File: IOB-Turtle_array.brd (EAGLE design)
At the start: 104.1 x 106.7 mm, 49 parts

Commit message: Added missing values
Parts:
- D1X11, D1X12, D1X13, D1X14: value (none) -> 4.7v
- R1X11, R1X12, R1X13, R1X14, R2X11, R2X12, R2X13, R2X14, R3X11, R3X12, R3X13, R3X14: value (none) -> 10k
- R4X11, R4X12, R4X13, R4X14: value (none) -> 1k0
- R5X11, R5X12, R5X13, R5X14, R6X11, R6X12, R6X13, R6X14, R7X11, R7X12, R7X13, R7X14: value (none) -> 200R
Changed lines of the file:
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@@
 </autorouter>
 <elements>
-<element name="D1X11" library="SPCoast" package="SOT23-3" value="" x="63.5" y="12.7" rot="R180"/>
+<element name="D1X11" library="SPCoast" package="SOT23-3" value="4.7v" x="63.5" y="12.7" rot="R180"/>
 <element name="FID1X11" library="SPCoast" package="FIDUCIAL_1MM" value="" x="41.275" y="10.16"/>
 <element name="FID2X11" library="SPCoast" package="FIDUCIAL_1MM" value="" x="76.835" y="27.305"/>
 <element name="J1X11" library="SPCoast" package="RJ24-INVERTED-PINS" value="" x="32.385" y="17.78" rot="R90"/>
-<element name="R1X11" library="SPCoast" package="0805-RES" value="" x="58.42" y="24.13" rot="R270"/>
-<element name="R2X11" library="SPCoast" package="0805-RES" value="" x="54.61" y="24.13" rot="R270"/>
-<element name="R3X11" library="SPCoast" package="0805-RES" value="" x="50.8" y="24.13" rot="R270"/>
-<element name="R4X11" library="SPCoast" package="0805-RES" value="" x="54.61" y="12.7"/>
-<element name="R5X11" library="SPCoast" package="0805-RES" value="" x="43.18" y="19.05" rot="R180"/>
-<element name="R6X11" library="SPCoast" package="0805-RES" value="" x="43.18" y="16.51" rot="R180"/>
-<element name="R7X11" library="SPCoast" package="0805-RES" value="" x="43.18" y="21.59" rot="R180"/>
+<element name="R1X11" library="SPCoast" package="0805-RES" value="10k" x="58.42" y="24.13" rot="R270"/>
+<element name="R2X11" library="SPCoast" package="0805-RES" value="10k" x="54.61" y="24.13" rot="R270"/>
+<element name="R3X11" library="SPCoast" package="0805-RES" value="10k" x="50.8" y="24.13" rot="R270"/>
+<element name="R4X11" library="SPCoast" package="0805-RES" value="1k0" x="54.61" y="12.7"/>
+<element name="R5X11" library="SPCoast" package="0805-RES" value="200R" x="43.18" y="19.05" rot="R180"/>
+<element name="R6X11" library="SPCoast" package="0805-RES" value="200R" x="43.18" y="16.51" rot="R180"/>
+<element name="R7X11" library="SPCoast" package="0805-RES" value="200R" x="43.18" y="21.59" rot="R180"/>
 <element name="U$1X11" library="SPCoast" package="IO4-IOB" value="" x="25.4" y="8.89"/>
-<element name="D1X12" library="SPCoast" package="SOT23-3" value="" x="63.5" y="33.02" rot="R180"/>
+<element name="D1X12" library="SPCoast" package="SOT23-3" value="4.7v" x="63.5" y="33.02" rot="R180"/>
 <element name="FID1X12" library="SPCoast" package="FIDUCIAL_1MM" value="" x="41.275" y="30.48"/>
 <element name="FID2X12" library="SPCoast" package="FIDUCIAL_1MM" value="" x="76.835" y="47.625"/>
 <element name="J1X12" library="SPCoast" package="RJ24-INVERTED-PINS" value="" x="32.385" y="38.1" rot="R90"/>
-<element name="R1X12" library="SPCoast" package="0805-RES" value="" x="58.42" y="44.45" rot="R270"/>
-<element name="R2X12" library="SPCoast" package="0805-RES" value="" x="54.61" y="44.45" rot="R270"/>
-<element name="R3X12" library="SPCoast" package="0805-RES" value="" x="50.8" y="44.45" rot="R270"/>
-<element name="R4X12" library="SPCoast" package="0805-RES" value="" x="54.61" y="33.02"/>
-<element name="R5X12" library="SPCoast" package="0805-RES" value="" x="43.18" y="39.37" rot="R180"/>
-<element name="R6X12" library="SPCoast" package="0805-RES" value="" x="43.18" y="36.83" rot="R180"/>
-<element name="R7X12" library="SPCoast" package="0805-RES" value="" x="43.18" y="41.91" rot="R180"/>
+<element name="R1X12" library="SPCoast" package="0805-RES" value="10k" x="58.42" y="44.45" rot="R270"/>
+<element name="R2X12" library="SPCoast" package="0805-RES" value="10k" x="54.61" y="44.45" rot="R270"/>
+<element name="R3X12" library="SPCoast" package="0805-RES" value="10k" x="50.8" y="44.45" rot="R270"/>
+<element name="R4X12" library="SPCoast" package="0805-RES" value="1k0" x="54.61" y="33.02"/>
+<element name="R5X12" library="SPCoast" package="0805-RES" value="200R" x="43.18" y="39.37" rot="R180"/>
+<element name="R6X12" library="SPCoast" package="0805-RES" value="200R" x="43.18" y="36.83" rot="R180"/>
+<element name="R7X12" library="SPCoast" package="0805-RES" value="200R" x="43.18" y="41.91" rot="R180"/>
 <element name="U$1X12" library="SPCoast" package="IO4-IOB" value="" x="25.4" y="29.21"/>
-<element name="D1X13" library="SPCoast" package="SOT23-3" value="" x="63.5" y="53.34" rot="R180"/>
+<element name="D1X13" library="SPCoast" package="SOT23-3" value="4.7v" x="63.5" y="53.34" rot="R180"/>
 <element name="FID1X13" library="SPCoast" package="FIDUCIAL_1MM" value="" x="41.275" y="50.8"/>
 <element name="FID2X13" library="SPCoast" package="FIDUCIAL_1MM" value="" x="76.835" y="67.945"/>
 <element name="J1X13" library="SPCoast" package="RJ24-INVERTED-PINS" value="" x="32.385" y="58.42" rot="R90"/>
-<element name="R1X13" library="SPCoast" package="0805-RES" value="" x="58.42" y="64.77" rot="R270"/>
-<element name="R2X13" library="SPCoast" package="0805-RES" value="" x="54.61" y="64.77" rot="R270"/>
-<element name="R3X13" library="SPCoast" package="0805-RES" value="" x="50.8" y="64.77" rot="R270"/>
-<element name="R4X13" library="SPCoast" package="0805-RES" value="" x="54.61" y="53.34"/>
-<element name="R5X13" library="SPCoast" package="0805-RES" value="" x="43.18" y="59.69" rot="R180"/>
-<element name="R6X13" library="SPCoast" package="0805-RES" value="" x="43.18" y="57.15" rot="R180"/>
-<element name="R7X13" library="SPCoast" package="0805-RES" value="" x="43.18" y="62.23" rot="R180"/>
+<element name="R1X13" library="SPCoast" package="0805-RES" value="10k" x="58.42" y="64.77" rot="R270"/>
+<element name="R2X13" library="SPCoast" package="0805-RES" value="10k" x="54.61" y="64.77" rot="R270"/>
+<element name="R3X13" library="SPCoast" package="0805-RES" value="10k" x="50.8" y="64.77" rot="R270"/>
+<element name="R4X13" library="SPCoast" package="0805-RES" value="1k0" x="54.61" y="53.34"/>
+<element name="R5X13" library="SPCoast" package="0805-RES" value="200R" x="43.18" y="59.69" rot="R180"/>
+<element name="R6X13" library="SPCoast" package="0805-RES" value="200R" x="43.18" y="57.15" rot="R180"/>
+<element name="R7X13" library="SPCoast" package="0805-RES" value="200R" x="43.18" y="62.23" rot="R180"/>
 <element name="U$1X13" library="SPCoast" package="IO4-IOB" value="" x="25.4" y="49.53"/>
-<element name="D1X14" library="SPCoast" package="SOT23-3" value="" x="63.5" y="73.66" rot="R180"/>
+<element name="D1X14" library="SPCoast" package="SOT23-3" value="4.7v" x="63.5" y="73.66" rot="R180"/>
 <element name="FID1X14" library="SPCoast" package="FIDUCIAL_1MM" value="" x="41.275" y="71.12"/>
 <element name="FID2X14" library="SPCoast" package="FIDUCIAL_1MM" value="" x="76.835" y="88.265"/>
 <element name="J1X14" library="SPCoast" package="RJ24-INVERTED-PINS" value="" x="32.385" y="78.74" rot="R90"/>
-<element name="R1X14" library="SPCoast" package="0805-RES" value="" x="58.42" y="85.09" rot="R270"/>
-<element name="R2X14" library="SPCoast" package="0805-RES" value="" x="54.61" y="85.09" rot="R270"/>
-<element name="R3X14" library="SPCoast" package="0805-RES" value="" x="50.8" y="85.09" rot="R270"/>
-<element name="R4X14" library="SPCoast" package="0805-RES" value="" x="54.61" y="73.66"/>
-<element name="R5X14" library="SPCoast" package="0805-RES" value="" x="43.18" y="80.01" rot="R180"/>
-<element name="R6X14" library="SPCoast" package="0805-RES" value="" x="43.18" y="77.47" rot="R180"/>
-<element name="R7X14" library="SPCoast" package="0805-RES" value="" x="43.18" y="82.55" rot="R180"/>
+<element name="R1X14" library="SPCoast" package="0805-RES" value="10k" x="58.42" y="85.09" rot="R270"/>
+<element name="R2X14" library="SPCoast" package="0805-RES" value="10k" x="54.61" y="85.09" rot="R270"/>
+<element name="R3X14" library="SPCoast" package="0805-RES" value="10k" x="50.8" y="85.09" rot="R270"/>
+<element name="R4X14" library="SPCoast" package="0805-RES" value="1k0" x="54.61" y="73.66"/>
+<element name="R5X14" library="SPCoast" package="0805-RES" value="200R" x="43.18" y="80.01" rot="R180"/>
+<element name="R6X14" library="SPCoast" package="0805-RES" value="200R" x="43.18" y="77.47" rot="R180"/>
+<element name="R7X14" library="SPCoast" package="0805-RES" value="200R" x="43.18" y="82.55" rot="R180"/>
 <element name="U$1X14" library="SPCoast" package="IO4-IOB" value="" x="25.4" y="69.85"/>
 <element name="U$1X1" library="SPCoast" package="BOARD-DINRAIL-3.17IN-H4X-IOB" value="" x="0" y="0"/>

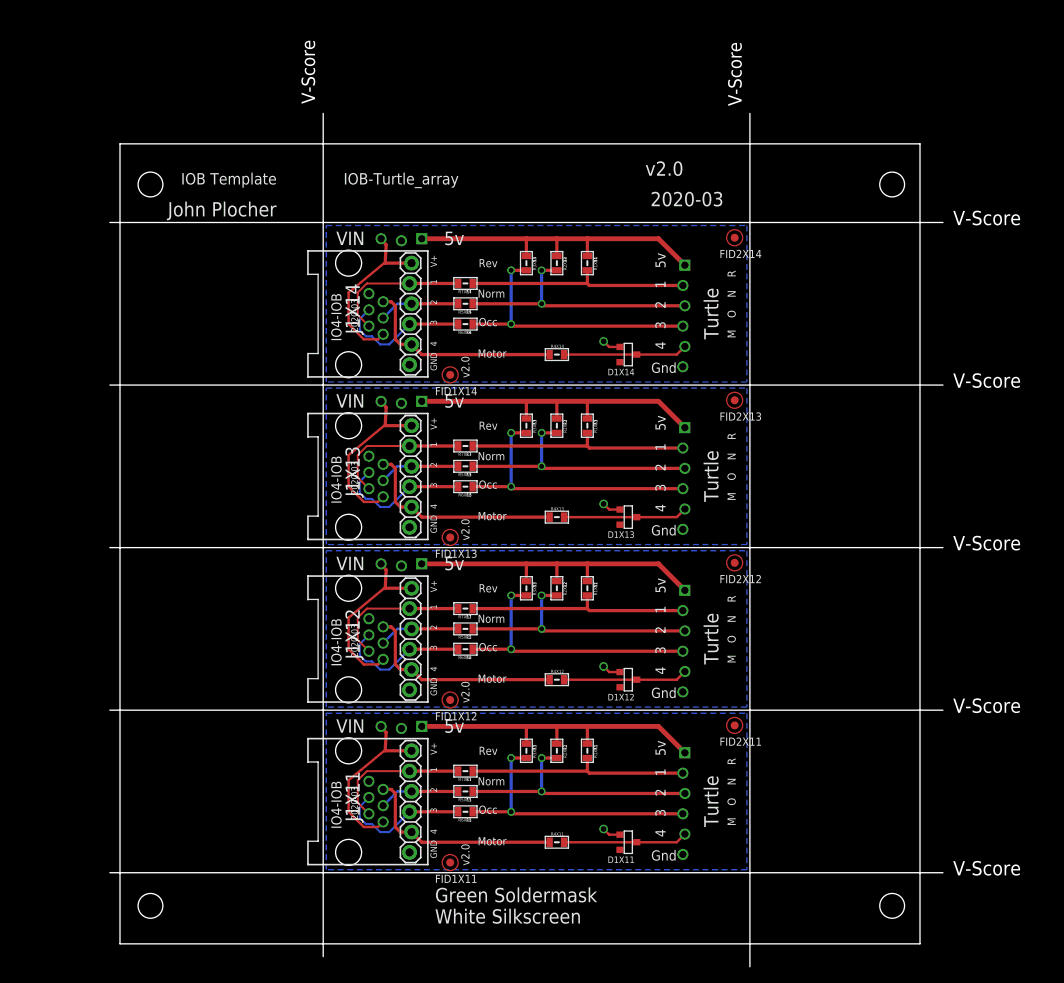
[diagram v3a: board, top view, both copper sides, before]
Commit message: add lpf on inputs, normalized silkscreen layout across IOBs
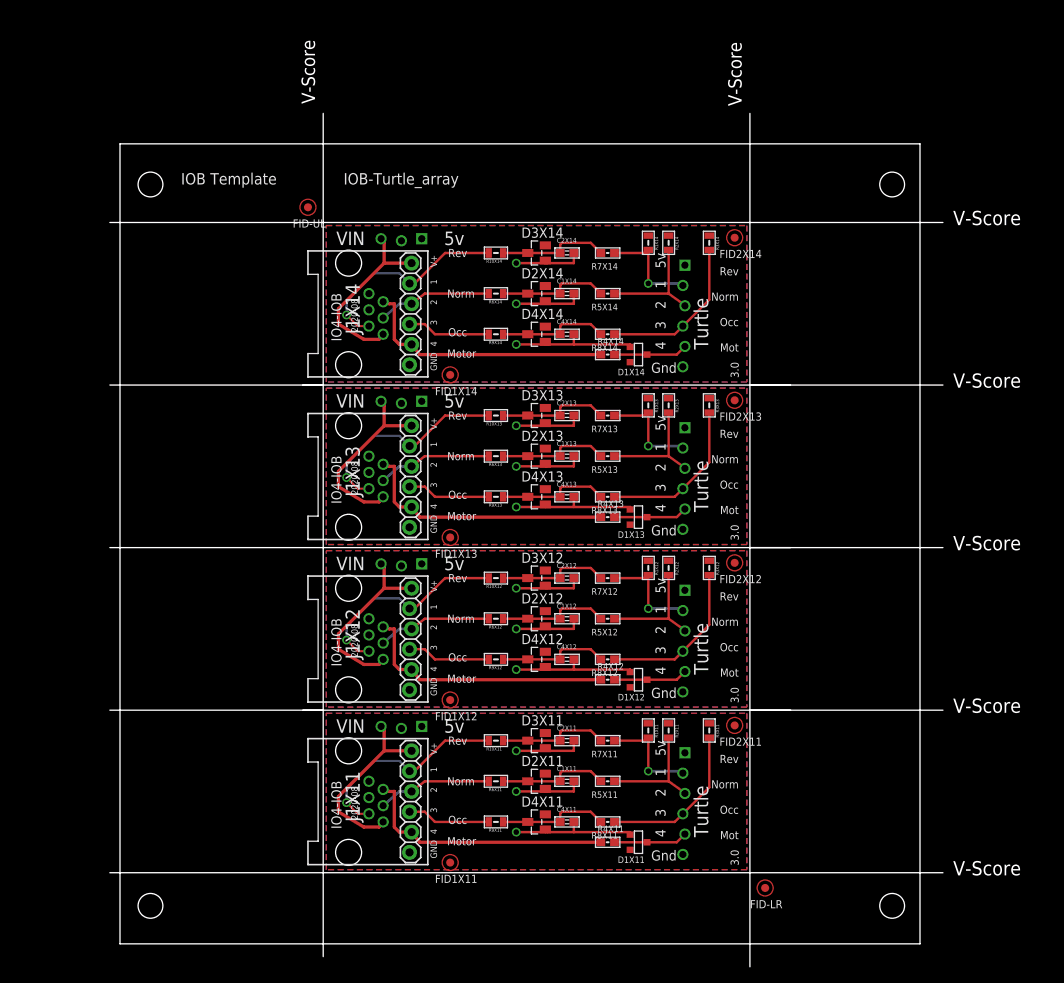
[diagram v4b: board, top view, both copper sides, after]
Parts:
- added C1X11, C1X12, C1X13, C1X14, C2X11, C2X12, C2X13, C2X14, C4X11, C4X12, C4X13, C4X14: 0.01uF, SPCoast:0603-CAP
- added D2X11, D2X12, D2X13, D2X14, D3X11, D3X12, D3X13, D3X14, D4X11, D4X12, D4X13, D4X14: BAT54S, SPCoast:SOT23
- added FID-LR, FID-UL: FIDUCIAL, SPCoast:FIDUCIAL_1MM
- added R10X11, R10X12, R10X13, R10X14, R9X11, R9X12, R9X13, R9X14: 82R, SPCoast:0805-RES
- added R8X11, R8X12, R8X13, R8X14: 1K0, SPCoast:0603-RES
- FID1X11, FID1X12, FID1X13, FID1X14, FID2X11, FID2X12, FID2X13, FID2X14: value (none) -> FIDUCIAL
- J1X11, J1X12, J1X13, J1X14: value (none) -> RJ12/6
- R4X11, R4X12, R4X13, R4X14: value 1k0 -> 1K0; device SPCoast:0805-RES -> SPCoast:0603-RES
- R5X11, R5X12, R5X13, R5X14, R7X11, R7X12, R7X13, R7X14: value 200R -> 1K0; device SPCoast:0805-RES -> SPCoast:0603-RES
- R6X11, R6X12, R6X13, R6X14: value 200R -> 82R
- U$1X11, U$1X12, U$1X13, U$1X14: value (none) -> CONNECTOR-IO4-IOBBARE
- moved R3X11 23.0 mm to (73.7, 26.7)
- moved R3X12 23.0 mm to (73.7, 47.0)
- moved R3X13 23.0 mm to (73.7, 67.3)
- moved R3X14 23.0 mm to (73.7, 87.6)
- moved R7X13 18.2 mm to (61.0, 66.0)
- moved R7X11 18.2 mm to (61.0, 25.4)
- moved R7X12 18.2 mm to (61.0, 45.7)
- moved R7X14 18.2 mm to (61.0, 86.4)
- moved R5X11 17.8 mm to (61.0, 20.3)
- moved R5X12 17.8 mm to (61.0, 40.6)
- moved R5X13 17.8 mm to (61.0, 61.0)
- moved R5X14 17.8 mm to (61.0, 81.3)
- moved R2X11 14.2 mm to (68.6, 26.7)
- moved R2X13 14.2 mm to (68.6, 67.3)
- moved R2X12 14.2 mm to (68.6, 47.0)
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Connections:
- removed net IO4-4X11: J1X11.4, J1X11.4@1, R6X11.2
- removed net IO4-4X12: J1X12.4, J1X12.4@1, R6X12.2
- removed net IO4-4X13: J1X13.4, J1X13.4@1, R6X13.2
- removed net IO4-4X14: J1X14.4, J1X14.4@1, R6X14.2
- new net N$14X11: C4X11.1, D4X11.3, R8X11.2, R9X11.1
- new net N$14X12: C4X12.1, D4X12.3, R8X12.2, R9X12.1
- new net N$14X13: C4X13.1, D4X13.3, R8X13.2, R9X13.1
- new net N$14X14: C4X14.1, D4X14.3, R8X14.2, R9X14.1
- new net N$1X11: J1X11.4, J1X11.4@1, R9X11.2
- new net N$1X12: J1X12.4, J1X12.4@1, R9X12.2
- new net N$1X13: J1X13.4, J1X13.4@1, R9X13.2
- new net N$1X14: J1X14.4, J1X14.4@1, R9X14.2
- new net N$2X11: C1X11.1, D2X11.3, R5X11.2, R6X11.1
- new net N$2X12: C1X12.1, D2X12.3, R5X12.2, R6X12.1
- new net N$2X13: C1X13.1, D2X13.3, R5X13.2, R6X13.1
- new net N$2X14: C1X14.1, D2X14.3, R5X14.2, R6X14.1
- new net N$3X11: C2X11.1, D3X11.3, R10X11.1, R7X11.2
- new net N$3X12: C2X12.1, D3X12.3, R10X12.1, R7X12.2
- new net N$3X13: C2X13.1, D3X13.3, R10X13.1, R7X13.2
- new net N$3X14: C2X14.1, D3X14.3, R10X14.1, R7X14.2
- net !OCCX11: now also R8X11.1; no longer R6X11.1
- net !OCCX12: now also R8X12.1; no longer R6X12.1
- net !OCCX13: now also R8X13.1; no longer R6X13.1
- net !OCCX14: now also R8X14.1; no longer R6X14.1
- net GNDX11: now also C1X11.2, C2X11.2, C4X11.2, D2X11.1, D3X11.1, D4X11.1
- net GNDX12: now also C1X12.2, C2X12.2, C4X12.2, D2X12.1, D3X12.1, D4X12.1
- net GNDX13: now also C1X13.2, C2X13.2, C4X13.2, D2X13.1, D3X13.1, D4X13.1
- net GNDX14: now also C1X14.2, C2X14.2, C4X14.2, D2X14.1, D3X14.1, D4X14.1
- net IO4-2X11: now also R10X11.2; no longer R7X11.2
- net IO4-2X12: now also R10X12.2; no longer R7X12.2
- net IO4-2X13: now also R10X13.2; no longer R7X13.2
- net IO4-2X14: now also R10X14.2; no longer R7X14.2
- net IO4-3X11: now also R6X11.2; no longer R5X11.2
- net IO4-3X12: now also R6X12.2; no longer R5X12.2
- net IO4-3X13: now also R6X13.2; no longer R5X13.2
- net IO4-3X14: now also R6X14.2; no longer R5X14.2
- net VCCX11: now also D2X11.2, D3X11.2, D4X11.2
- net VCCX12: now also D2X12.2, D3X12.2, D4X12.2
- net VCCX13: now also D2X13.2, D3X13.2, D4X13.2
- net VCCX14: now also D2X14.2, D3X14.2, D4X14.2
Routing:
- net VCCX14: track 40.7 -> 0.00 mm
- net VCCX11: track 40.7 -> 0.00 mm
- net VCCX13: track 40.7 -> 0.00 mm
- net VCCX12: track 40.7 -> 0.00 mm
- net GNDX13: track 2.34 -> 34.6 mm, vias 1 -> 3
- net GNDX12: track 2.34 -> 34.6 mm, vias 1 -> 3
- net GNDX11: track 2.34 -> 34.6 mm, vias 1 -> 3
- net GNDX14: track 2.34 -> 34.6 mm, vias 1 -> 3
- net !NORMX13: track 32.7 -> 14.8 mm, vias 2 -> 0
- net !NORMX11: track 32.7 -> 14.8 mm, vias 2 -> 0
- net !NORMX12: track 32.7 -> 14.8 mm, vias 2 -> 0
- net !NORMX14: track 32.7 -> 14.8 mm, vias 2 -> 0
- net IO4-4X12: track 17.1 -> 0.00 mm
- net IO4-4X11: track 17.1 -> 0.00 mm
- net IO4-4X13: track 17.1 -> 0.00 mm
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- added copper zone on layer 1, net VCCX11
- added copper zone on layer 1, net VCCX12
- added copper zone on layer 1, net VCCX13
- added copper zone on layer 1, net VCCX14
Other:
- board text added: "2020-08"
- board text added: "3.0"
- board text added: "C1"
- board text added: "C2"
- board text added: "C4"
- board text added: "D2"
- board text added: "D3"
- board text added: "D4"
- board text added: "Green Header"
- board text added: "Mot"
- board text added: "R10"
- board text added: "R8"
- board text added: "R9"
- board text removed: "2020-03"
- board text removed: "M"
- board text removed: "N"
- board text removed: "O"
- board text removed: "R"
- board text removed: "v2.0"
